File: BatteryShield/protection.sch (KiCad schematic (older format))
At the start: 10 parts

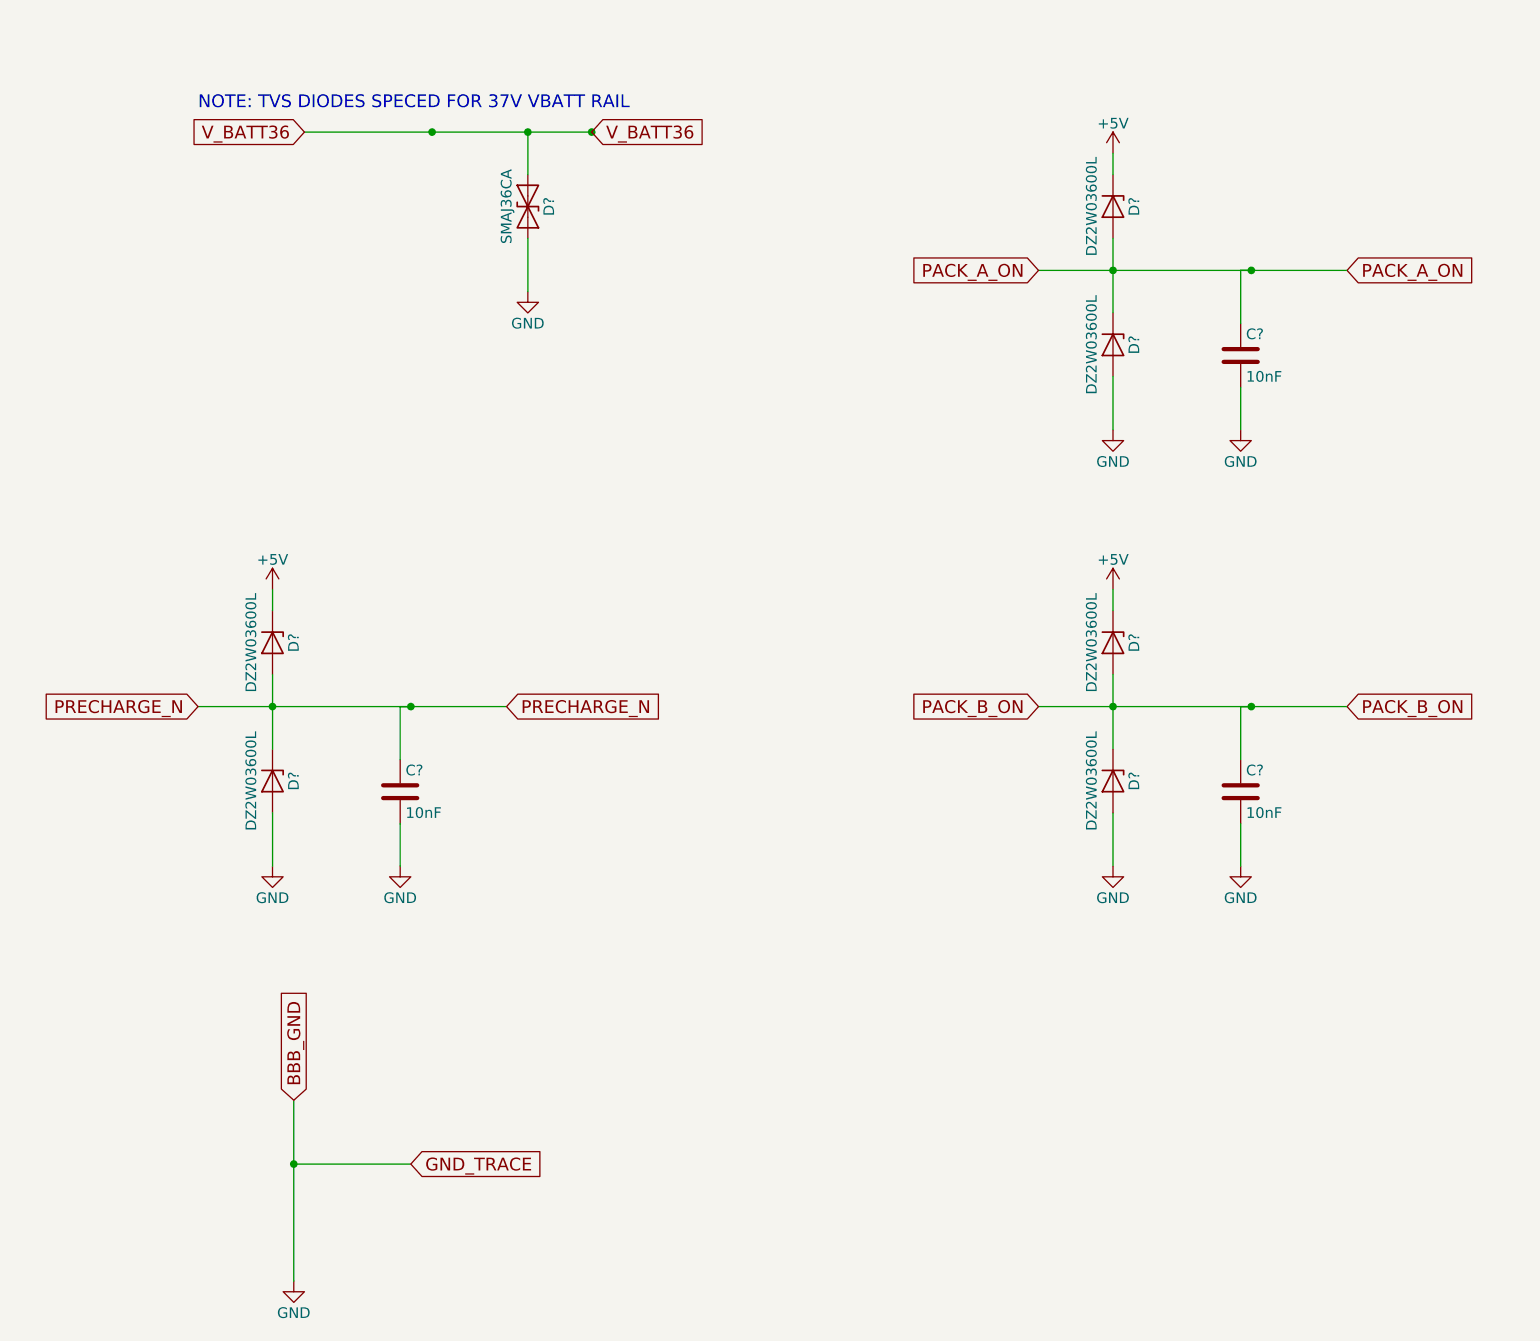
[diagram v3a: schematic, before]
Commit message: Did V.1 of layout; removed old circuits
gosh I need to do schoolwork
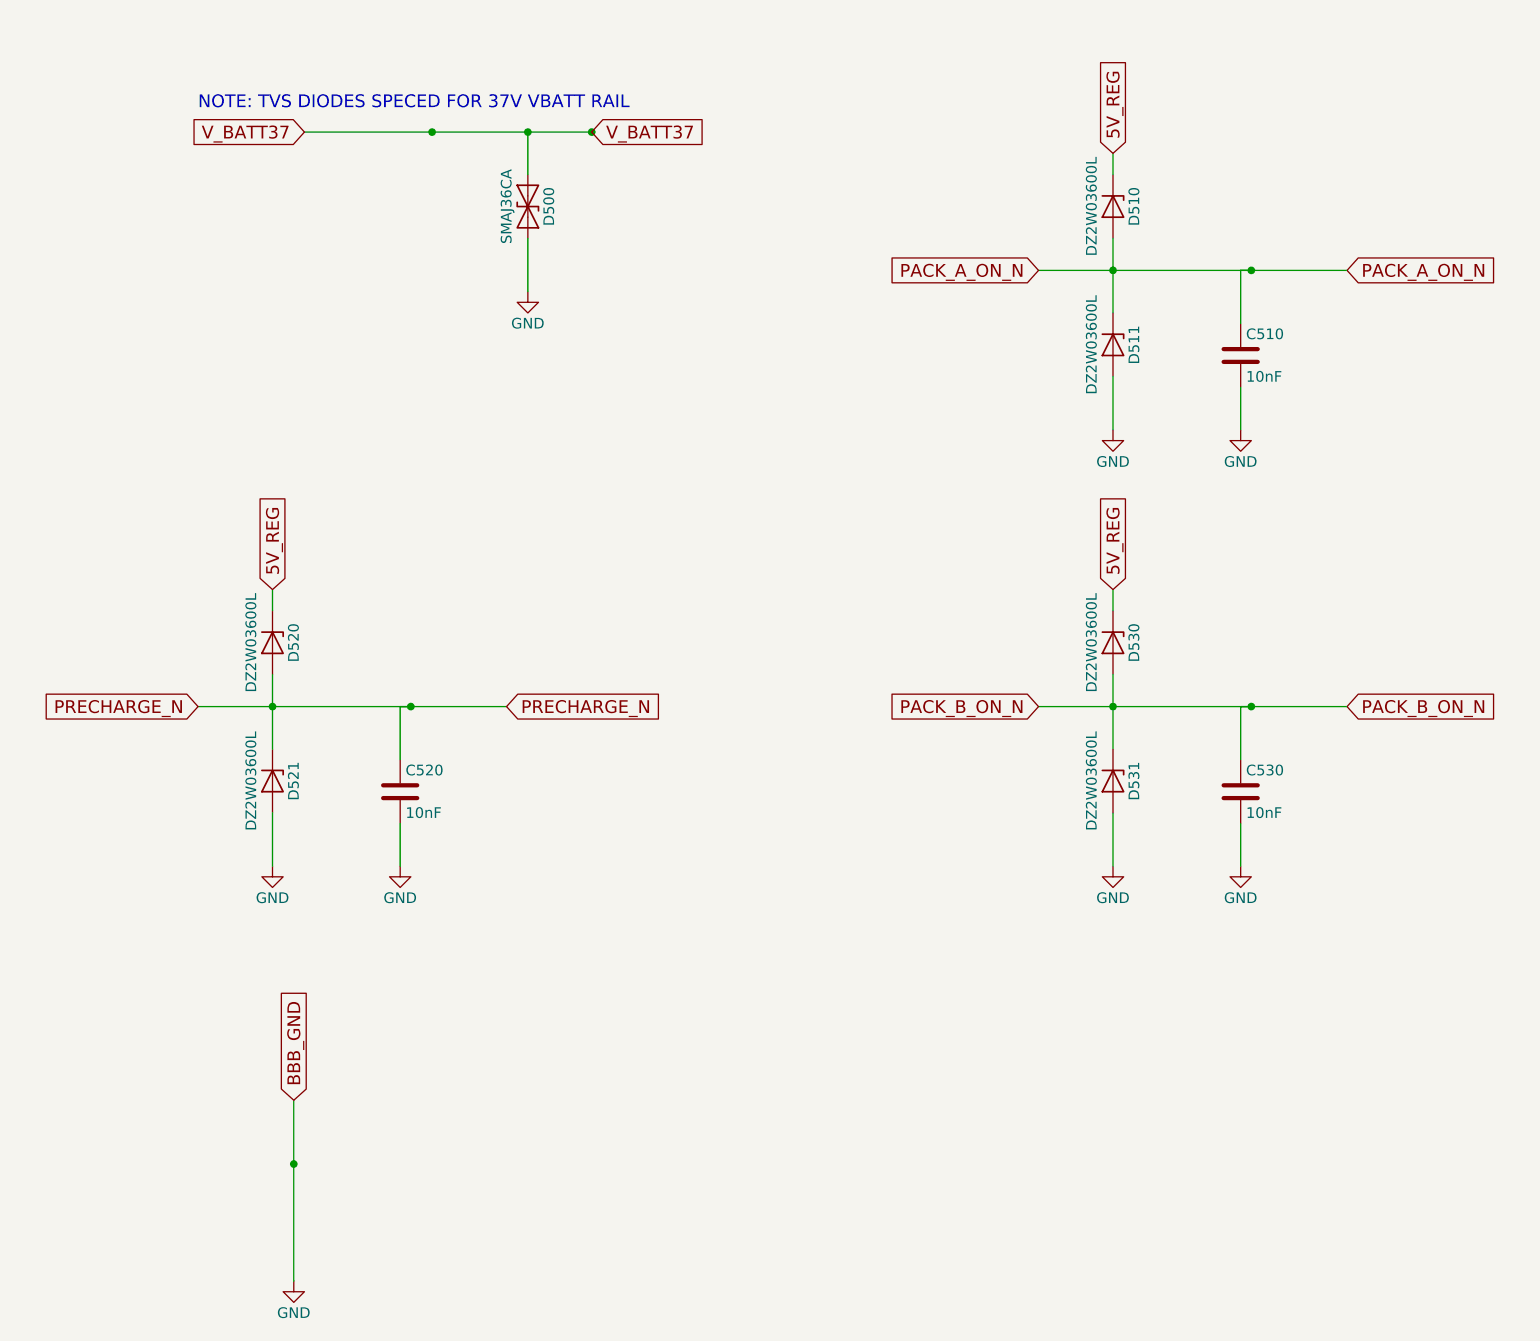
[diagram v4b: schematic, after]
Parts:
- gave numbers to parts that had none: 10
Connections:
- net +5V renamed 5V_REG
- net PACK_A_ON renamed PACK_A_ON_N
- net PACK_B_ON renamed PACK_B_ON_N
- net V_BATT36 renamed V_BATT37
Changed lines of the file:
@@
 LIBS:LTC4151IMS-1-PBF
 LIBS:sensors
+LIBS:powerRes
 LIBS:Battery_Shield-cache
 EELAYER 25 0
@@
 $Descr A4 11693 8268
 encoding utf-8
-Sheet 10 12
+Sheet 6 8
 Title ""
 Date ""
@@
 $EndDescr
 Text GLabel 3250 1200 0    60   Input ~ 0
-V_BATT36
+V_BATT37
 Text GLabel 4600 1200 2    60   Input ~ 0
-V_BATT36
-$Comp
-L D_TVS D?
+V_BATT37
+$Comp
+L D_TVS D500
 U 1 1 5B11F88F
 P 4300 1550
-F 0 "D?" H 4300 1650 50  0000 C CNN
+F 0 "D500" H 4300 1650 50  0000 C CNN
 F 1 "SMAJ36CA" H 4300 1450 50  0000 C CNN
 F 2 "Diodes_SMD:D_SMA" H 4300 1550 50  0001 C CNN
@@
 $EndComp
 $Comp
-L GND #PWR023
+L GND #PWR013
 U 1 1 5B11F8FB
 P 4300 1950
-F 0 "#PWR023" H 4300 1700 50  0001 C CNN
+F 0 "#PWR013" H 4300 1700 50  0001 C CNN
 F 1 "GND" H 4300 1800 50  0000 C CNN
 F 2 "" H 4300 1950 50  0001 C CNN
@@
 Connection ~ 3850 1200
 Connection ~ 4600 1200
-Wire Wire Line
-	4300 1400 4300 1200
 Connection ~ 4300 1200
 Wire Wire Line
@@
 Connection ~ 3100 3900
 $Comp
-L GND #PWR024
+L GND #PWR014
 U 1 1 5B12464E
 P 3100 4650
-F 0 "#PWR024" H 3100 4400 50  0001 C CNN
+F 0 "#PWR014" H 3100 4400 50  0001 C CNN
 F 1 "GND" H 3100 4500 50  0000 C CNN
 F 2 "" H 3100 4650 50  0001 C CNN
@@
 Connection ~ 3750 3900
 $Comp
-L GND #PWR025
+L GND #PWR015
 U 1 1 5B124921
 P 3700 4650
-F 0 "#PWR025" H 3700 4400 50  0001 C CNN
+F 0 "#PWR015" H 3700 4400 50  0001 C CNN
 F 1 "GND" H 3700 4500 50  0000 C CNN
 F 2 "" H 3700 4650 50  0001 C CNN
@@
 Wire Wire Line
 	3700 4650 3700 4450
-$Comp
-L +5V #PWR026
-U 1 1 5B124B04
-P 3100 3350
-F 0 "#PWR026" H 3100 3200 50  0001 C CNN
-F 1 "+5V" H 3100 3490 50  0000 C CNN
-F 2 "" H 3100 3350 50  0001 C CNN
-F 3 "" H 3100 3350 50  0001 C CNN
-	1    3100 3350
-	1    0    0    -1
-$EndComp
 Wire Wire Line
 	3100 3450 3100 3350
 Text GLabel 6700 1850 0    60   Input ~ 0
-PACK_A_ON
+PACK_A_ON_N
 Text GLabel 8150 1850 2    60   Input ~ 0
-PACK_A_ON
+PACK_A_ON_N
 Wire Wire Line
 	6700 1850 8150 1850
@@
 Connection ~ 7050 1850
 $Comp
-L GND #PWR027
+L GND #PWR016
 U 1 1 5B12518E
 P 7050 2600
-F 0 "#PWR027" H 7050 2350 50  0001 C CNN
+F 0 "#PWR016" H 7050 2350 50  0001 C CNN
 F 1 "GND" H 7050 2450 50  0000 C CNN
 F 2 "" H 7050 2600 50  0001 C CNN
@@
 	7050 2600 7050 2350
 $Comp
-L C C?
+L C C510
 U 1 1 5B125195
 P 7650 2250
-F 0 "C?" H 7675 2350 50  0000 L CNN
+F 0 "C510" H 7675 2350 50  0000 L CNN
 F 1 "10nF" H 7675 2150 50  0000 L CNN
 F 2 "Capacitors_SMD:C_0402" H 7688 2100 50  0001 C CNN
@@
 Connection ~ 7700 1850
 $Comp
-L GND #PWR028
+L GND #PWR017
 U 1 1 5B12519E
 P 7650 2600
-F 0 "#PWR028" H 7650 2350 50  0001 C CNN
+F 0 "#PWR017" H 7650 2350 50  0001 C CNN
 F 1 "GND" H 7650 2450 50  0000 C CNN
 F 2 "" H 7650 2600 50  0001 C CNN
@@
 Wire Wire Line
 	7650 2600 7650 2400
-$Comp
-L +5V #PWR029
-U 1 1 5B1251AB
-P 7050 1300
-F 0 "#PWR029" H 7050 1150 50  0001 C CNN
-F 1 "+5V" H 7050 1440 50  0000 C CNN
-F 2 "" H 7050 1300 50  0001 C CNN
-F 3 "" H 7050 1300 50  0001 C CNN
-	1    7050 1300
-	1    0    0    -1
-$EndComp
 Wire Wire Line
 	7050 1400 7050 1300
 Text GLabel 6700 3900 0    60   Input ~ 0
-PACK_B_ON
+PACK_B_ON_N
 Text GLabel 8150 3900 2    60   Input ~ 0
-PACK_B_ON
+PACK_B_ON_N
 Wire Wire Line
 	6700 3900 8150 3900
@@
 Connection ~ 7050 3900
 $Comp
-L GND #PWR030
+L GND #PWR018
 U 1 1 5B1252A9
 P 7050 4650
-F 0 "#PWR030" H 7050 4400 50  0001 C CNN
+F 0 "#PWR018" H 7050 4400 50  0001 C CNN
 F 1 "GND" H 7050 4500 50  0000 C CNN
 F 2 "" H 7050 4650 50  0001 C CNN
@@
 Connection ~ 7700 3900
 $Comp
-L GND #PWR031
+L GND #PWR019
 U 1 1 5B1252B9
 P 7650 4650
-F 0 "#PWR031" H 7650 4400 50  0001 C CNN
+F 0 "#PWR019" H 7650 4400 50  0001 C CNN
 F 1 "GND" H 7650 4500 50  0000 C CNN
 F 2 "" H 7650 4650 50  0001 C CNN
@@
 Wire Wire Line
 	7650 4650 7650 4450
-$Comp
-L +5V #PWR032
-U 1 1 5B1252C6
-P 7050 3350
-F 0 "#PWR032" H 7050 3200 50  0001 C CNN
-F 1 "+5V" H 7050 3490 50  0000 C CNN
-F 2 "" H 7050 3350 50  0001 C CNN
-F 3 "" H 7050 3350 50  0001 C CNN
-	1    7050 3350
-	1    0    0    -1
-$EndComp
 Wire Wire Line
 	7050 3450 7050 3350
 $Comp
-L GND #PWR033
+L GND #PWR020
 U 1 1 5B120B55
 P 3200 6600
-F 0 "#PWR033" H 3200 6350 50  0001 C CNN
+F 0 "#PWR020" H 3200 6350 50  0001 C CNN
 F 1 "GND" H 3200 6450 50  0000 C CNN
 F 2 "" H 3200 6600 50  0001 C CNN
@@
 Wire Wire Line
 	3200 5750 3200 6600
-Text GLabel 3750 6050 2    60   Input ~ 0
-GND_TRACE
-Wire Wire Line
-	3750 6050 3200 6050
 Connection ~ 3200 6050
 $Comp
-L D_Zener D?
+L D_Zener D521
 U 1 1 5B1245DC
 P 3100 4250
-F 0 "D?" H 3100 4350 50  0000 C CNN
+F 0 "D521" H 3100 4350 50  0000 C CNN
 F 1 "DZ2W03600L" H 3100 4150 50  0000 C CNN
 F 2 "Diodes_SMD:D_1206" H 3100 4250 50  0001 C CNN
@@
 $EndComp
 $Comp
-L D_Zener D?
+L D_Zener D531
 U 1 1 5B29E487
 P 7050 4250
-F 0 "D?" H 7050 4350 50  0000 C CNN
+F 0 "D531" H 7050 4350 50  0000 C CNN
 F 1 "DZ2W03600L" H 7050 4150 50  0000 C CNN
 F 2 "Diodes_SMD:D_1206" H 7050 4250 50  0001 C CNN
@@
 $EndComp
 $Comp
-L D_Zener D?
+L D_Zener D511
 U 1 1 5B29E4E1
 P 7050 2200
-F 0 "D?" H 7050 2300 50  0000 C CNN
+F 0 "D511" H 7050 2300 50  0000 C CNN
 F 1 "DZ2W03600L" H 7050 2100 50  0000 C CNN
 F 2 "Diodes_SMD:D_1206" H 7050 2200 50  0001 C CNN
@@
 $EndComp
 $Comp
-L D_Zener D?
+L D_Zener D520
 U 1 1 5B29E546
 P 3100 3600
-F 0 "D?" H 3100 3700 50  0000 C CNN
+F 0 "D520" H 3100 3700 50  0000 C CNN
 F 1 "DZ2W03600L" H 3100 3500 50  0000 C CNN
 F 2 "Diodes_SMD:D_1206" H 3100 3600 50  0001 C CNN
@@
 $EndComp
 $Comp
-L D_Zener D?
+L D_Zener D530
 U 1 1 5B29E588
 P 7050 3600
-F 0 "D?" H 7050 3700 50  0000 C CNN
+F 0 "D530" H 7050 3700 50  0000 C CNN
 F 1 "DZ2W03600L" H 7050 3500 50  0000 C CNN
 F 2 "Diodes_SMD:D_1206" H 7050 3600 50  0001 C CNN
@@
 $EndComp
 $Comp
-L D_Zener D?
+L D_Zener D510
 U 1 1 5B29E5FF
 P 7050 1550
-F 0 "D?" H 7050 1650 50  0000 C CNN
+F 0 "D510" H 7050 1650 50  0000 C CNN
 F 1 "DZ2W03600L" H 7050 1450 50  0000 C CNN
 F 2 "Diodes_SMD:D_1206" H 7050 1550 50  0001 C CNN
@@
 $EndComp
 $Comp
-L C C?
+L C C530
 U 1 1 5B29E6BD
 P 7650 4300
-F 0 "C?" H 7675 4400 50  0000 L CNN
+F 0 "C530" H 7675 4400 50  0000 L CNN
 F 1 "10nF" H 7675 4200 50  0000 L CNN
 F 2 "Capacitors_SMD:C_0402" H 7688 4150 50  0001 C CNN
@@
 $EndComp
 $Comp
-L C C?
+L C C520
 U 1 1 5B29E73C
 P 3700 4300
-F 0 "C?" H 3725 4400 50  0000 L CNN
+F 0 "C520" H 3725 4400 50  0000 L CNN
 F 1 "10nF" H 3725 4200 50  0000 L CNN
 F 2 "Capacitors_SMD:C_0402" H 3738 4150 50  0001 C CNN
@@
 	1    0    0    -1
 $EndComp
+Wire Wire Line
+	4300 1400 4300 1200
+Text GLabel 3100 3350 1    60   Input ~ 0
+5V_REG
+Text GLabel 7050 3350 1    60   Input ~ 0
+5V_REG
+Text GLabel 7050 1300 1    60   Input ~ 0
+5V_REG
 $EndSCHEMATC

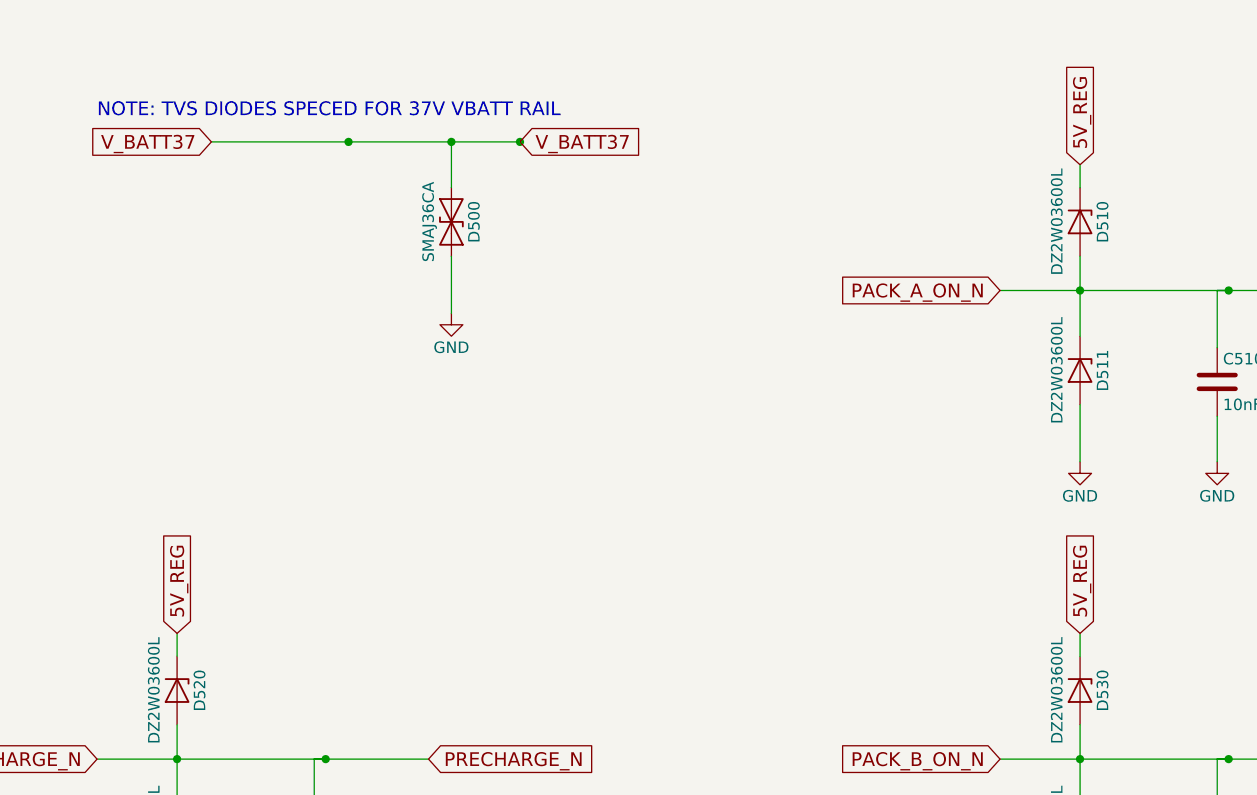
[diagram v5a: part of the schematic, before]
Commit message: Changed BBB regulation voltage from 5V to 3.3V
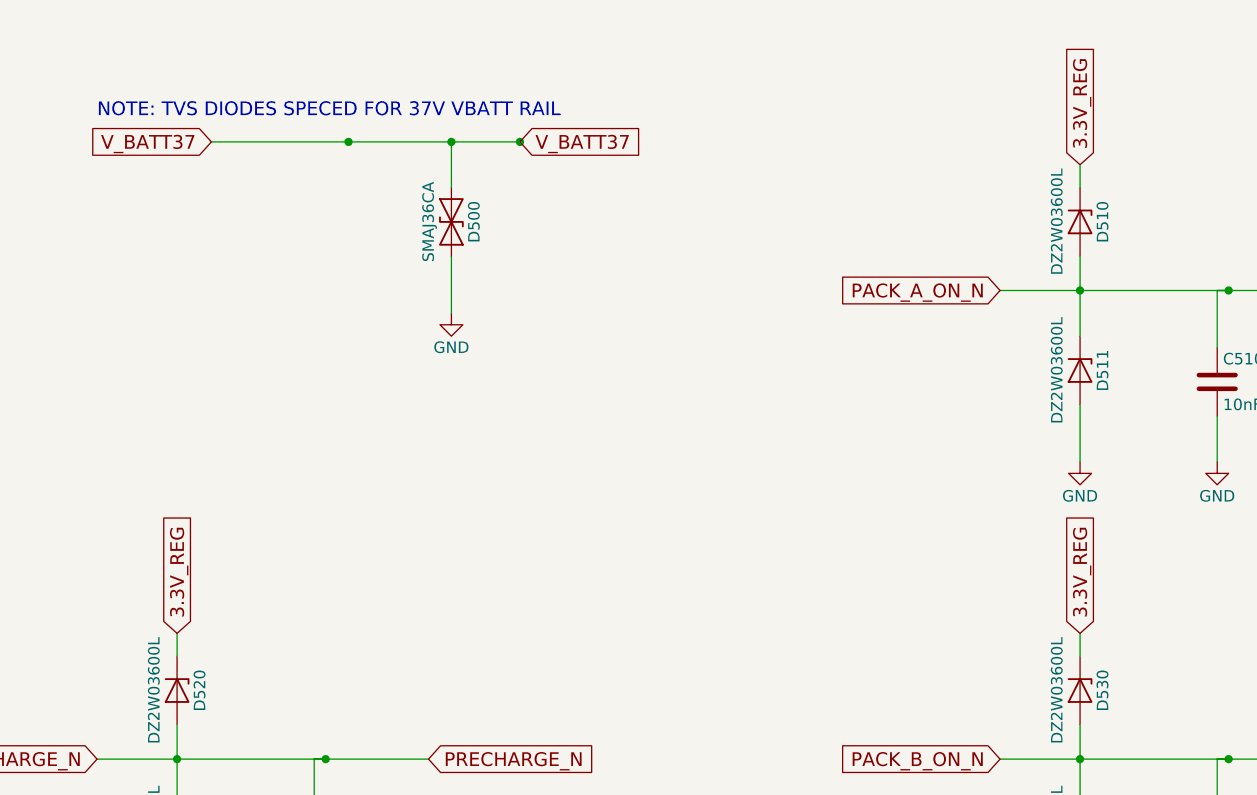
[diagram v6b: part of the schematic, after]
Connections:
- net 5V_REG renamed 3.3V_REG
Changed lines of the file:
@@
 Wire Wire Line
 	4300 1400 4300 1200
+Text GLabel 7050 1300 1    60   Input ~ 0
+3.3V_REG
+Text GLabel 7050 3350 1    60   Input ~ 0
+3.3V_REG
 Text GLabel 3100 3350 1    60   Input ~ 0
-5V_REG
-Text GLabel 7050 3350 1    60   Input ~ 0
-5V_REG
-Text GLabel 7050 1300 1    60   Input ~ 0
-5V_REG
+3.3V_REG
 $EndSCHEMATC
